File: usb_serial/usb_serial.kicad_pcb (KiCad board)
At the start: 2 copper layers, 18 x 30 mm, 13 parts, among them J1 47589-1001, J3 Conn_01x04_Pin, U1 FT232RL

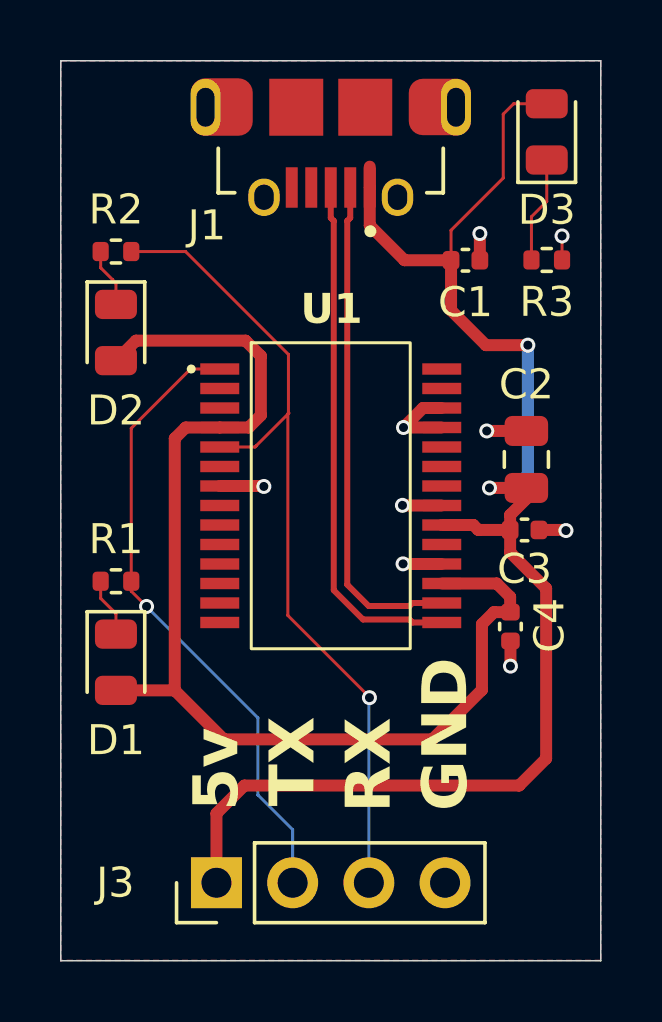
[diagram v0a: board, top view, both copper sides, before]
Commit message: JLCPCB adaptation - USB part changed
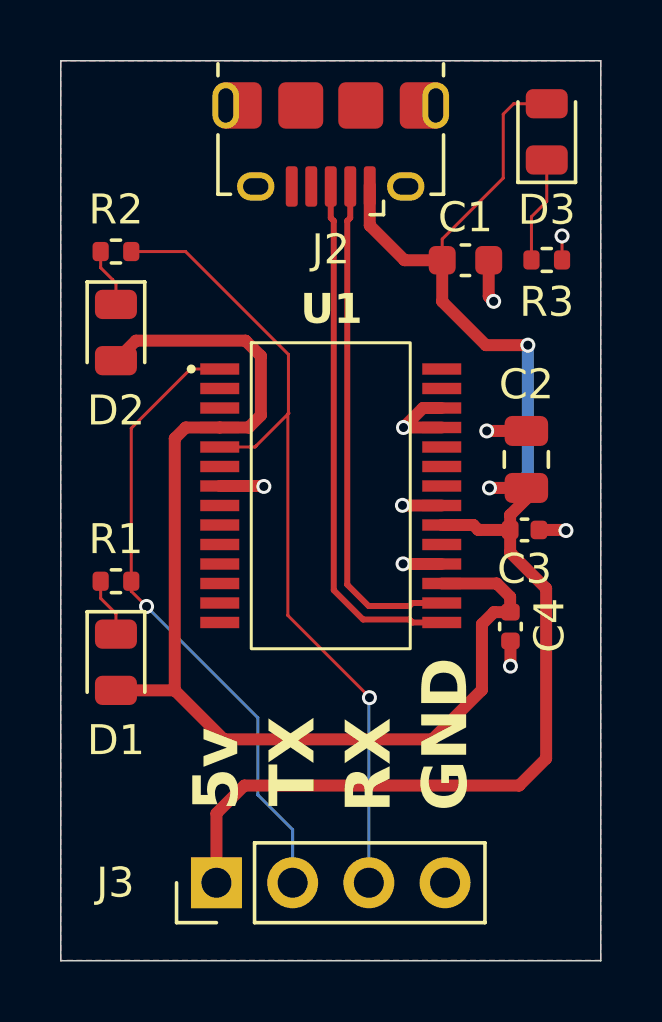
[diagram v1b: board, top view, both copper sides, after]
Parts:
- removed J1: 47589-1001, user_footprints:MOLEX_47589-1001
- added J2: USB_B_Micro, Connector_USB:USB_Micro-B_Amphenol_10118194-0001LF_Horizontal, F.Cu at (139.0, 62.8)
- C1: footprint Capacitor_SMD:C_0402_1005Metric -> Capacitor_SMD:C_0603_1608Metric
- R3: value 2.2k -> 1k
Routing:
- net +5V: track 50.2 -> 49.5 mm
- net GND: track 11.7 -> 12.2 mm

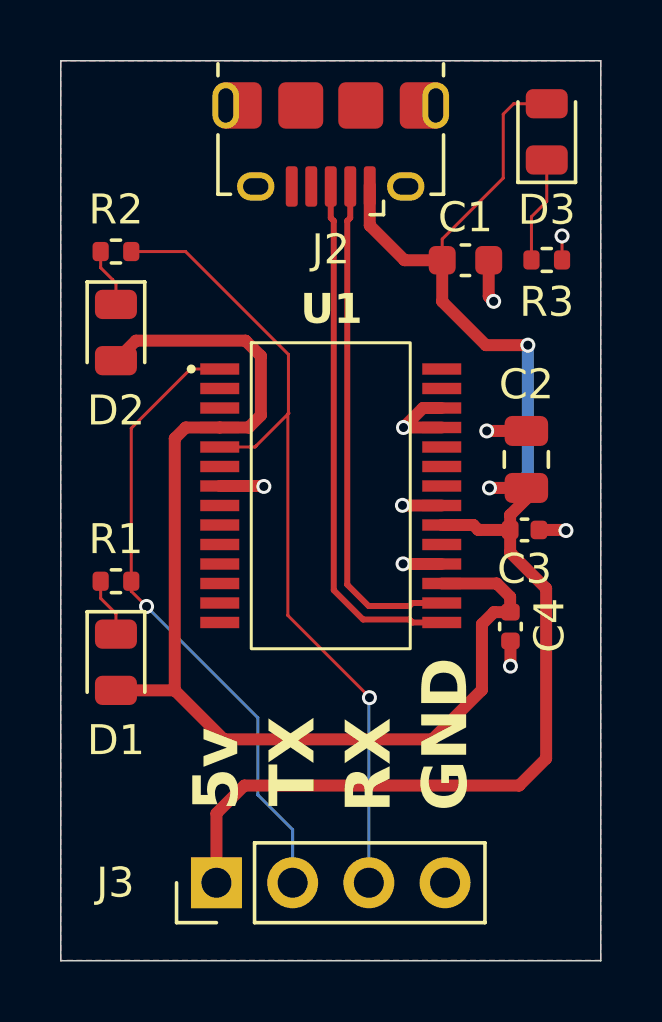
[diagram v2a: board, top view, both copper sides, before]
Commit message: Layout fix - Stub removal
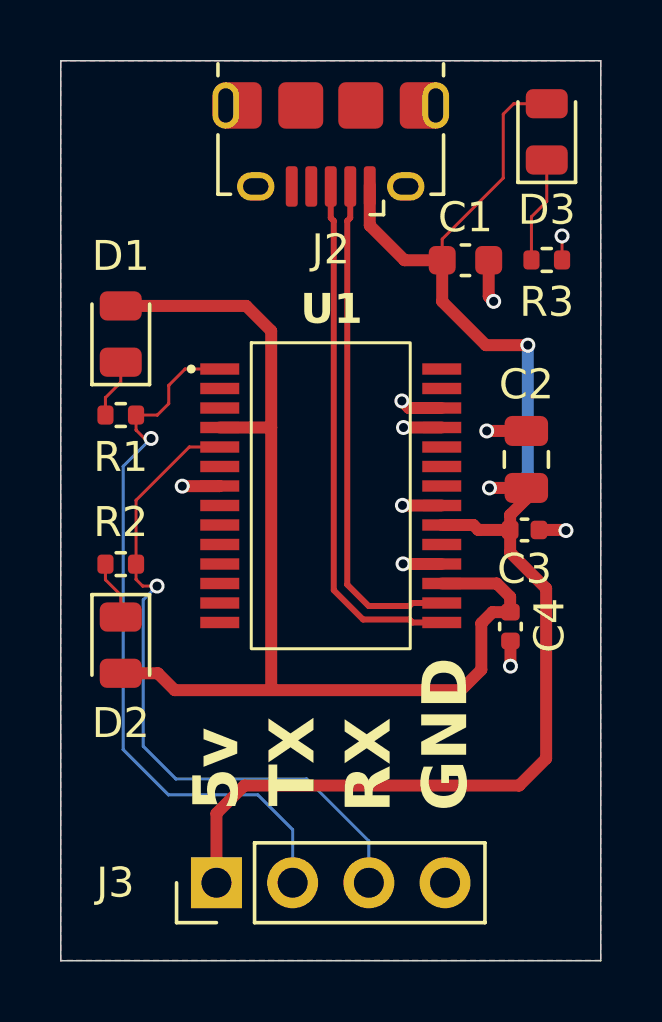
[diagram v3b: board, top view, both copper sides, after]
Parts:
- moved D1 10.9 mm to (132.0, 69.1), turned to 90 degrees
- moved D2 10.4 mm to (132.0, 79.5)
- moved R2 10.4 mm to (132.0, 76.8)
- moved R1 5.54 mm to (132.0, 71.8)
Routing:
- net /UART_RX: track 28.2 -> 22.7 mm
- net /UART_TX: track 21.1 -> 24.2 mm
- net +3.3V: track 38.7 -> 37.2 mm
- net GND: track 12.2 -> 11.9 mm, vias 9 -> 10
